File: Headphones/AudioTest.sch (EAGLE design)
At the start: 0 parts

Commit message: Started audio testing schematic
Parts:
- added J1, J2, J3: SJ-43516, Master:SJ-43516
- added J4, J5, J6, J7: (no value), SparkFun-Connectors:M06LOCK
- added K1, K2: CPC1117N, Master:CPC1117N
- added U1: FSA553, Master:FSA553
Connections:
- new net N$1: J2.LEFT, J3.LEFT, J5.6, J6.1
- new net N$10: J1.GND, J4.2
- new net N$11: J1.RIGHT, J4.3
- new net N$12: J1.RIGHT_NC, J4.4
- new net N$13: J1.LEFT_NC, J4.5
- new net N$14: J1.LEFT, J4.6
- new net N$15: K1.A
- new net N$16: K1.C, K2.A
- new net N$17: K2.C
- new net N$2: J2.RIGHT, J3.RIGHT, J5.3, J6.4
- new net N$3: J2.GND, J3.GND, J5.2, J6.5
- new net N$4: J2.MIC, J3.MIC, J5.1, J6.6
- new net N$5: J2.RIGHT_NC, J5.4
- new net N$6: J2.LEFT_NC, J5.5
- new net N$7: J3.LEFT_NC, J6.2
- new net N$8: J3.RIGHT_NC, J6.3
- new net N$9: J1.MIC, J4.1

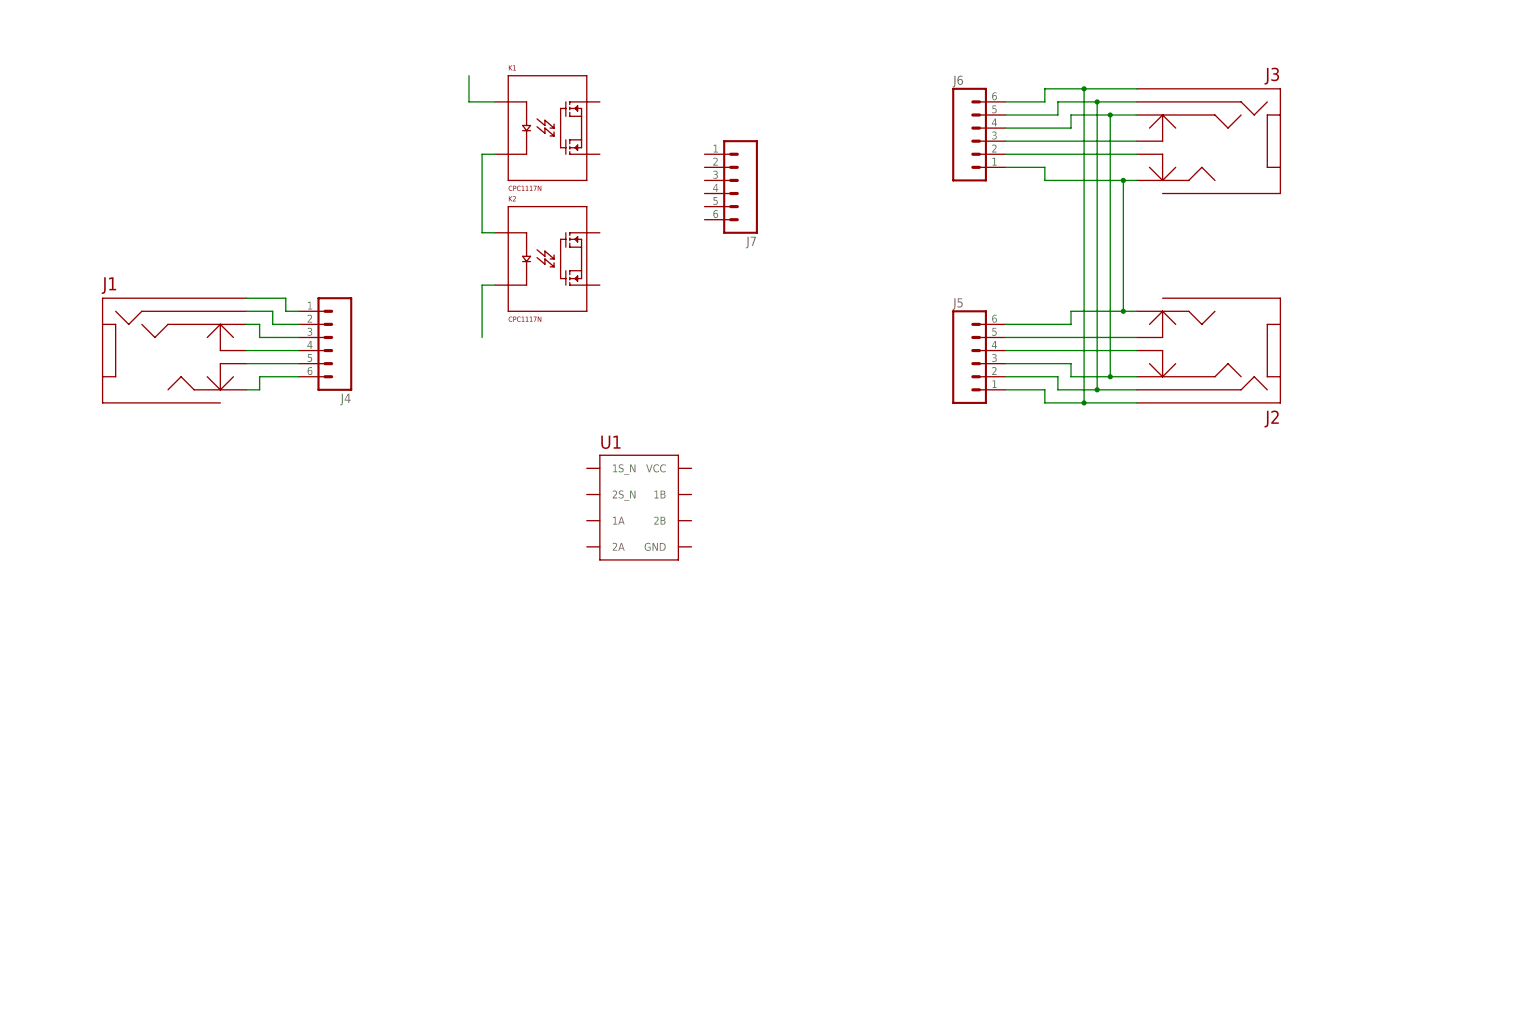
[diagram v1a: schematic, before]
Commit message: Created components and completed most of audio test schematic
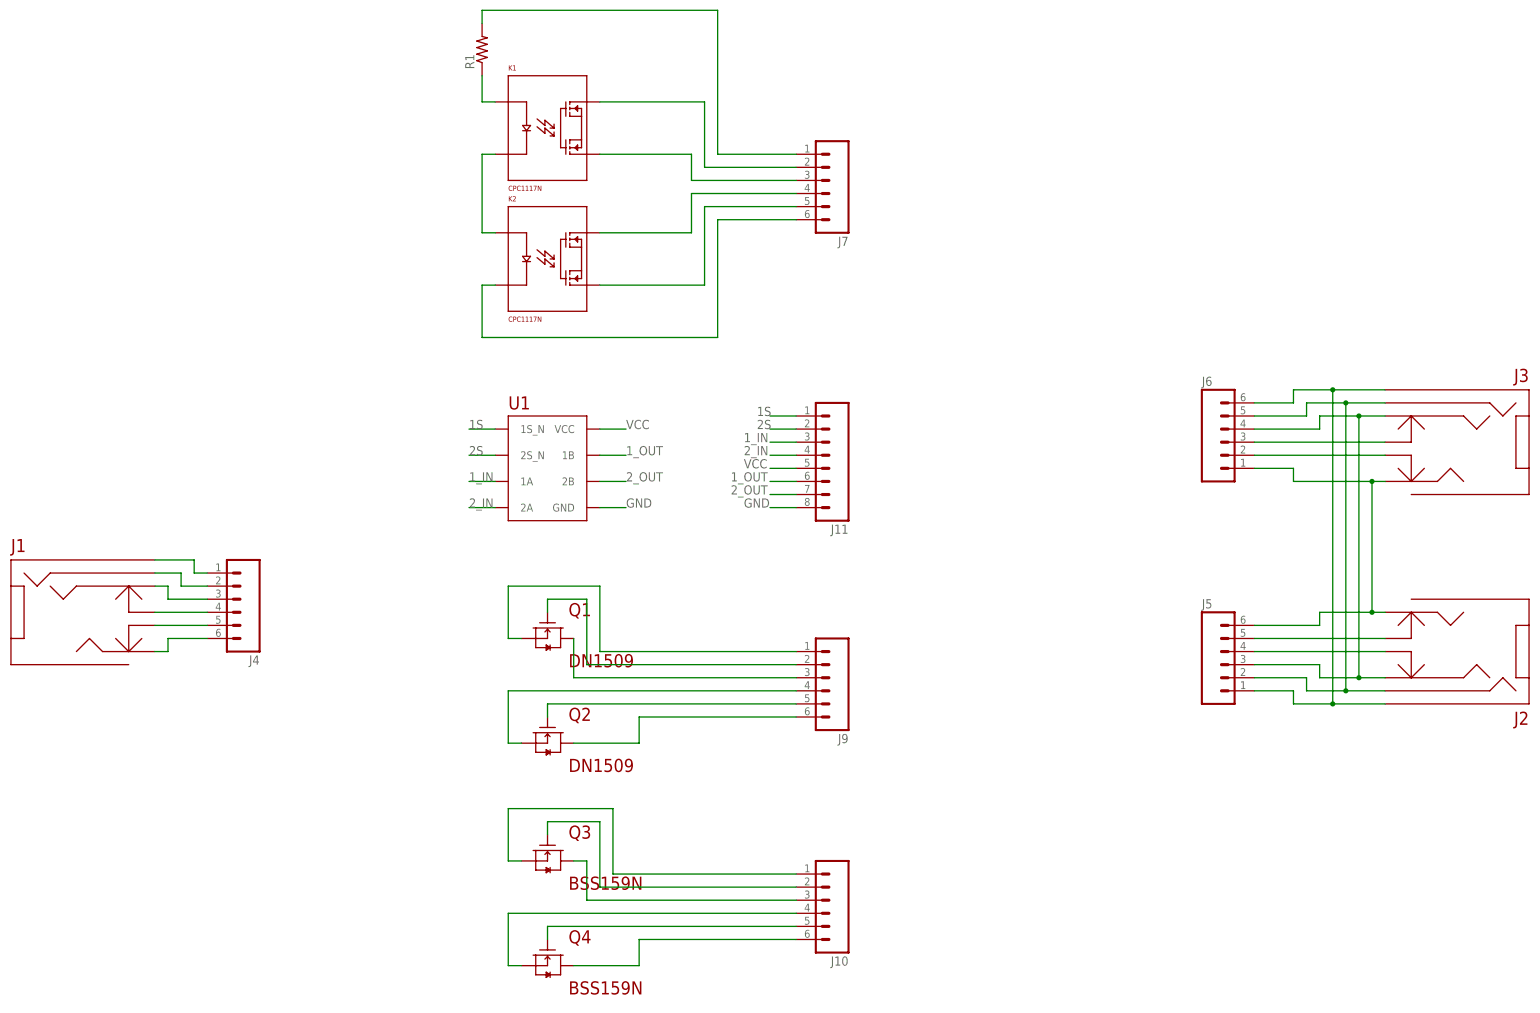
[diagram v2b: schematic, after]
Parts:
- added J10, J9: (no value), SparkFun-Connectors:M06LOCK
- added J11: (no value), SparkFun-Connectors:M08LOCK
- added Q1, Q2: DN1509, Master:DN1509
- added Q3, Q4: BSS159N, Master:BSS159N
- added R1: (no value), resistor:R-US_R0805
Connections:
- new net 1S: J11.1, U1.1S_N
- new net 1_IN: J11.3, U1.1A
- new net 1_OUT: J11.6, U1.1B
- new net 2S: J11.2, U1.2S_N
- new net 2_IN: J11.4, U1.2A
- new net 2_OUT: J11.7, U1.2B
- new net GND: J11.8, U1.GND
- new net N$18: J9.6, Q2.D
- new net N$19: J9.5, Q2.G
- new net N$20: J9.4, Q2.S
- new net N$21: J9.3, Q1.D
- new net N$22: J9.2, Q1.G
- new net N$23: J9.1, Q1.S
- new net N$24: J10.6, Q4.D
- new net N$25: J10.5, Q4.G
- new net N$26: J10.4, Q4.S
- new net N$27: J10.3, Q3.D
- new net N$28: J10.2, Q3.G
- new net N$29: J10.1, Q3.S
- new net N$30: J7.5, K2.LOAD2
- new net N$31: J7.4, K2.LOAD1
- new net N$32: J7.2, K1.LOAD1
- new net N$33: J7.3, K1.LOAD2
- new net R_GND: J7.6, K2.C
- new net VCC: J11.5, U1.VCC
- net N$15: now also R1.1
- net N$17: now also J7.1, R1.2; no longer K2.C
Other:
- moved on the sheet: J1, J2, J3, J4, J5, J6, J7, U1

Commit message: Adding Amazon Dash CAM files and added outline to schematic
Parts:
- added C1, C2, C3: (no value), resistor:C-EUC1210
- added J12, J13, J14, J8: (no value), SparkFun-Connectors:M06LOCK
- added R2, R3, R4: (no value), resistor:R-US_M0805
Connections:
- net N$1 renamed 2_L
- net N$11 renamed 1_R
- net N$12 renamed 1_R_SW
- net N$13 renamed 1_L_SW
- net N$14 renamed 1_L
- net N$17 renamed R_V+
- net N$18 renamed D2
- net N$19 renamed G2
- net N$2 renamed 2_R
- net N$20 renamed S2
- net N$21 renamed D1
- net N$22 renamed G1
- net N$23 renamed S1
- net N$24 renamed D4
- net N$25 renamed G4
- net N$26 renamed S4
- net N$27 renamed D3
- net N$28 renamed G3
- net N$29 renamed S3
- net N$30 renamed R_OUT2
- net N$31 renamed R_IN2
- net N$32 renamed R_IN1
- net N$33 renamed R_OUT1
- net N$4 renamed 2_M
- net N$5 renamed 2_R_SW
- net N$6 renamed 2_L_SW
- net N$7 renamed 3_SW_L
- net N$8 renamed 3_SW_R
- net N$9 renamed 1_M
- new net AGND: J1.GND, J2.GND, J3.GND, J4.2, J5.2, J6.5
- new net N$34: C2.2, J8.3, J8.4
- new net N$35: C1.2, J8.1, J8.2
- new net N$36: C1.1, J12.5, J12.6
- new net N$37: C2.1, J12.3, J12.4
- new net N$38: J14.1, J14.2, R4.1
- new net N$39: J13.5, J13.6, R4.2
- new net N$40: J13.3, J13.4, R3.2
- new net N$41: J13.1, J13.2, R2.2
- new net N$42: J14.5, J14.6, R2.1
- new net N$43: J14.3, J14.4, R3.1
- net 1S: now also J11.3; no longer J11.1
- net 1_IN: now also J11.5; no longer J11.3
- net 1_OUT: now also J11.7; no longer J11.6
- net 2S: now also J11.1; no longer J11.2
- net 2_OUT: now also J11.8; no longer J11.7
- net GND: now also J11.2; no longer J11.8
- net N$10: now also C3.2, J8.5, J8.6; no longer J1.GND, J4.2
- net N$3: now also C3.1, J12.1, J12.2; no longer J2.GND, J3.GND, J5.2, J6.5
- net VCC: now also J11.6; no longer J11.5
